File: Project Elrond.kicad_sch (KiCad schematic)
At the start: 23 parts, among them U1 OPA827, U2 OPA827, U3 OPA827

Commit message: Remove OS-specific file paths from kicad_sch
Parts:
- U1, U2, U3: Spice_Lib_File spice\OPA827.LIB -> OPA827.LIB
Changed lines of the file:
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@@
       (effects (font (size 1.27 1.27)) hide)
     )
-    (property "Spice_Lib_File" "spice\\OPA827.LIB" (id 7) (at 76.2 98.425 0)
+    (property "Spice_Lib_File" "OPA827.LIB" (id 7) (at 76.2 98.425 0)
       (effects (font (size 1.27 1.27)) hide)
     )
@@
       (effects (font (size 1.27 1.27)) hide)
     )
-    (property "Spice_Lib_File" "spice\\OPA827.LIB" (id 7) (at 160.02 100.965 0)
+    (property "Spice_Lib_File" "OPA827.LIB" (id 7) (at 160.02 100.965 0)
       (effects (font (size 1.27 1.27)) hide)
     )
@@
       (effects (font (size 1.27 1.27)) hide)
     )
-    (property "Spice_Lib_File" "spice\\OPA827.LIB" (id 7) (at 243.84 103.505 0)
+    (property "Spice_Lib_File" "OPA827.LIB" (id 7) (at 243.84 103.505 0)
       (effects (font (size 1.27 1.27)) hide)
     )

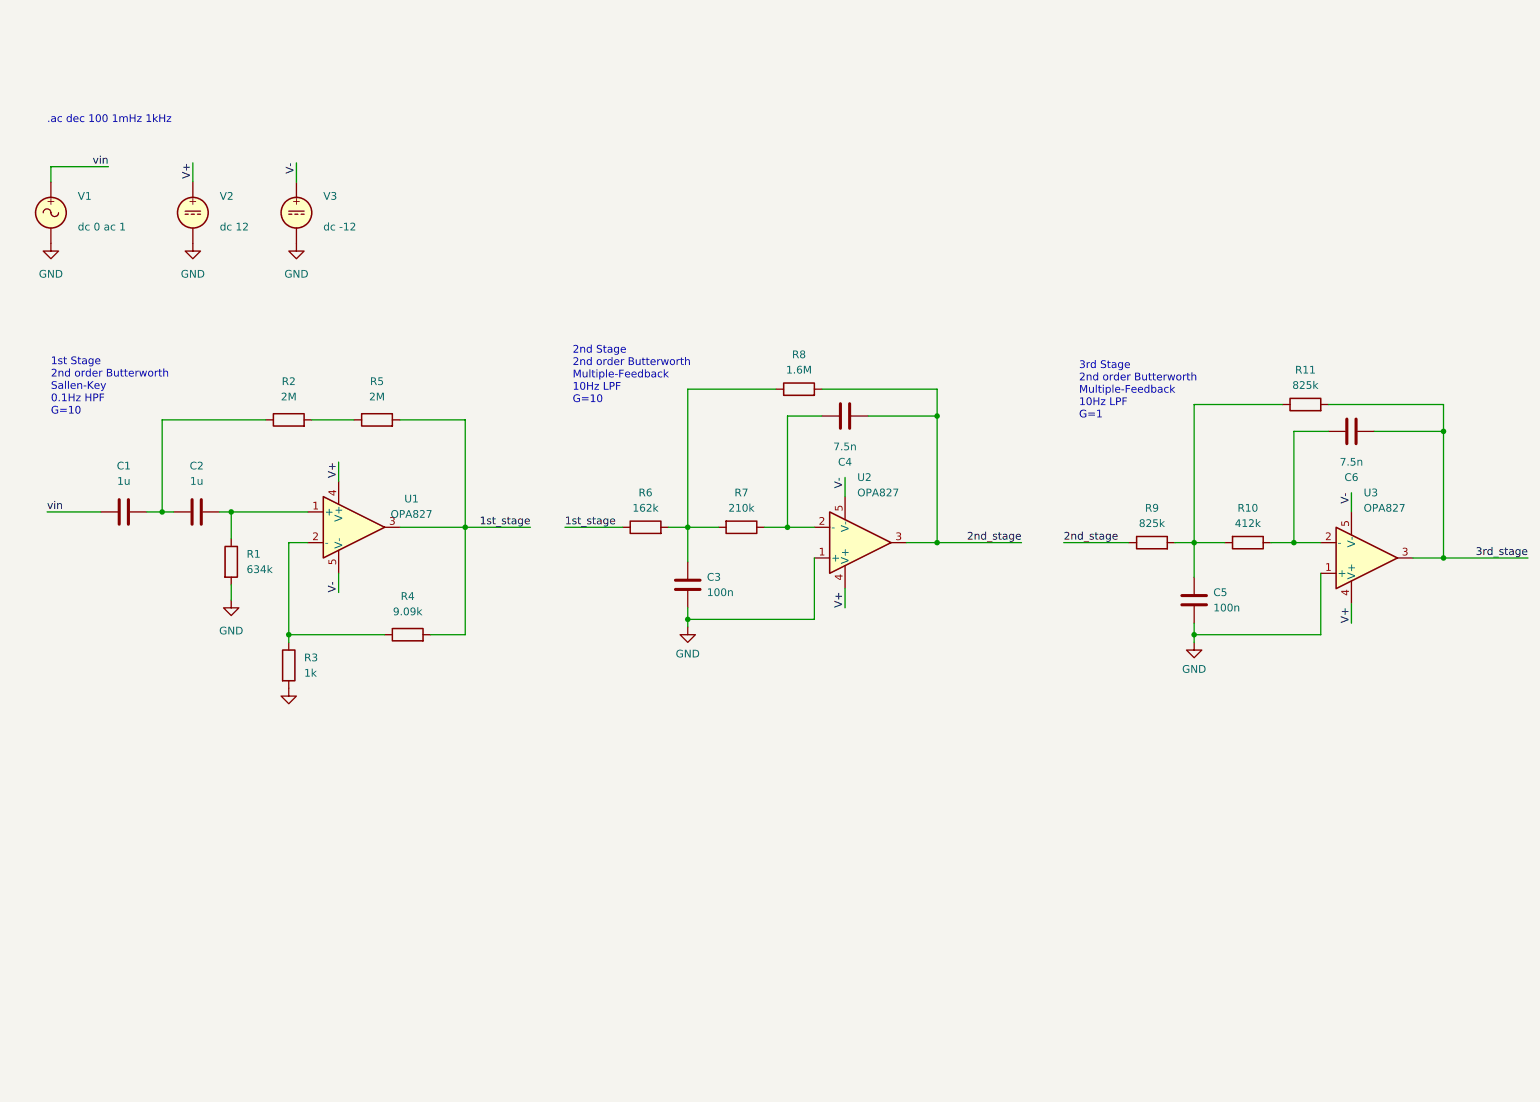
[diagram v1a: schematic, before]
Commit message: Use UA741 instead of the pricier OPA amplifier
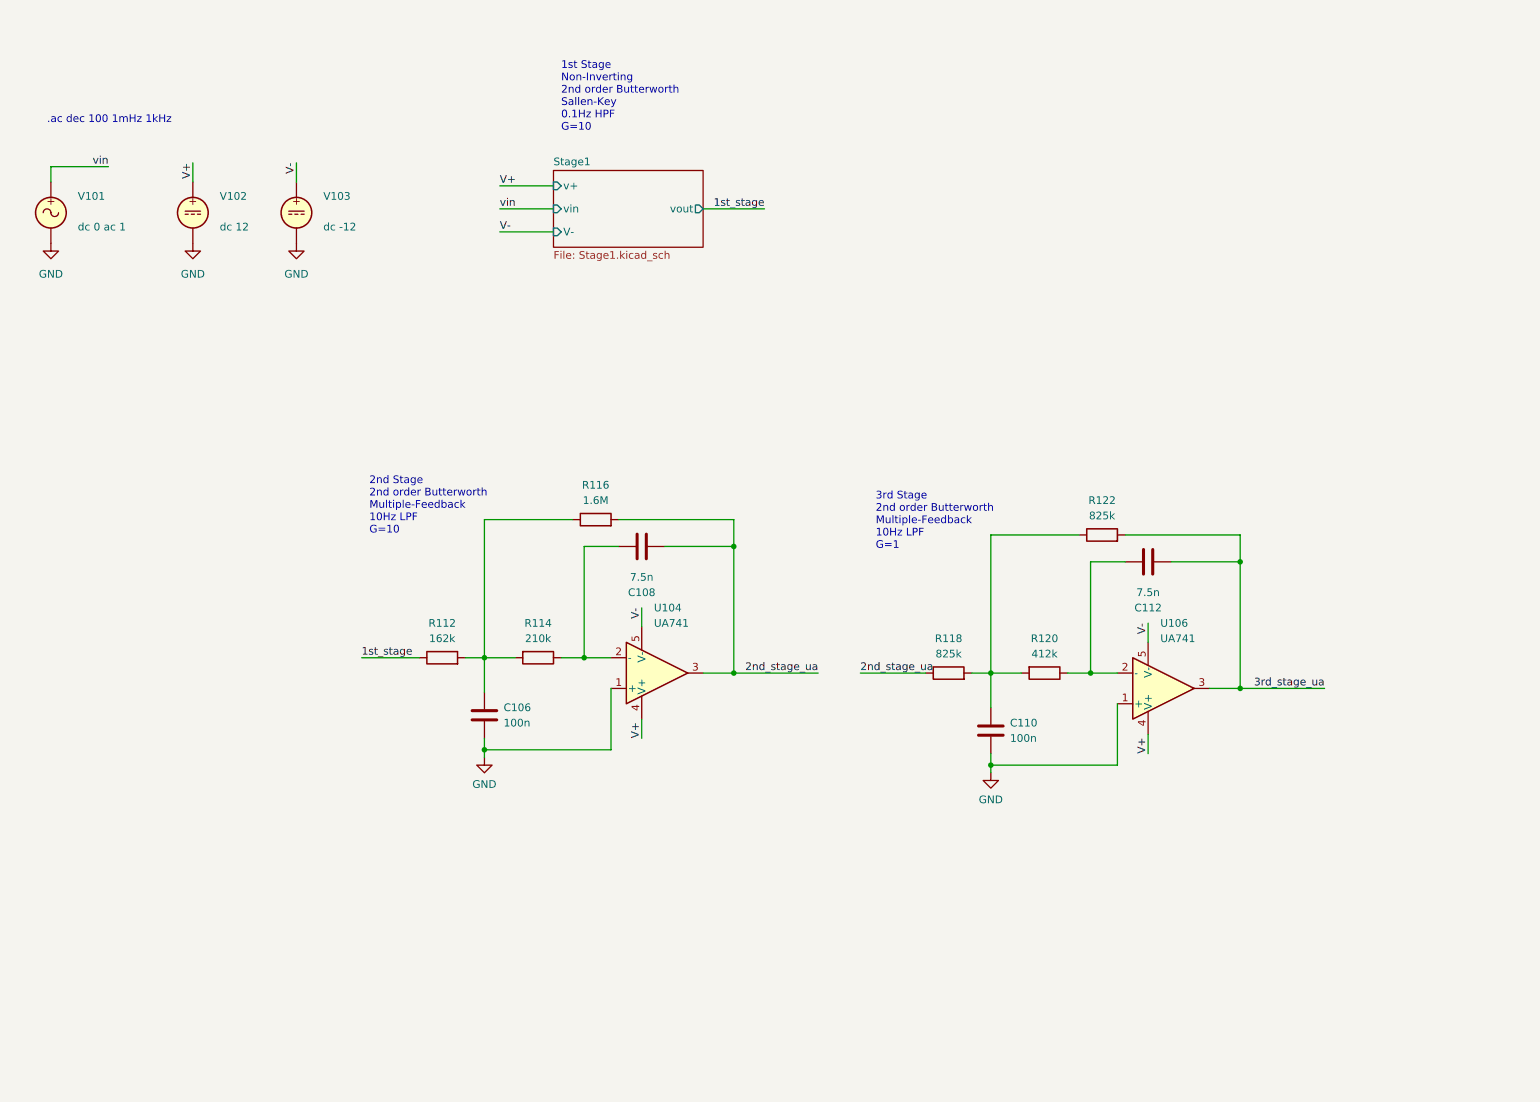
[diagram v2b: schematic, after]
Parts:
- removed C1, C2: 1u, symbol Device:C
- removed C3, C5: 100n, symbol Device:C
- removed C4, C6: 7.5n, symbol Device:C
- removed R1: 634k, symbol Device:R
- removed R10: 412k, symbol Device:R
- removed R11, R9: 825k, symbol Device:R
- removed R2, R5: 2M, symbol Device:R
- removed R3: 1k, symbol Device:R
- removed R4: 9.09k, symbol Device:R
- removed R6: 162k, symbol Device:R
- removed R7: 210k, symbol Device:R
- removed R8: 1.6M, symbol Device:R
- removed U1, U2, U3: OPA827, symbol Simulation_SPICE:OPAMP
- added C106, C110: 100n, symbol Device:C
- added C108, C112: 7.5n, symbol Device:C
- added R112: 162k, symbol Device:R
- added R114: 210k, symbol Device:R
- added R116: 1.6M, symbol Device:R
- added R118, R122: 825k, symbol Device:R
- added R120: 412k, symbol Device:R
- added U104, U106: UA741, symbol Simulation_SPICE:OPAMP
- renumbered V1 to V101, V2 to V102, V3 to V103
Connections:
- net 1st_stage: now also R112.1
- net GND: now also C106.2, C110.2, U104.1 (+), U106.1 (+)
- net V+: now also U104.4 (V+), U106.4 (V+)
- net V-: now also U104.5 (V-), U106.5 (V-)
- new net: C110.1, R118.2, R120.2, R122.1
- new net: C112.1, R120.1, U106.2 (-)
- new net: C108.1, R114.1, U104.2 (-)
- new net: C106.1, R112.2, R114.2, R116.1
- new net 2nd_stage_ua: C108.2, R116.2, R118.1, U104.3
- new net 3rd_stage_ua: C112.2, R122.2, U106.3
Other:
- added sheet Stage1 (Stage1.kicad_sch)
- note added: "1st Stage Non-Inverting 2nd order Butterworth Sallen-Key 0.1Hz HPF G=10"
- note removed: "1st Stage 2nd order Butterworth Sallen-Key 0.1Hz HPF G=10"

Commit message: Present an initial structure for multiple simulation support
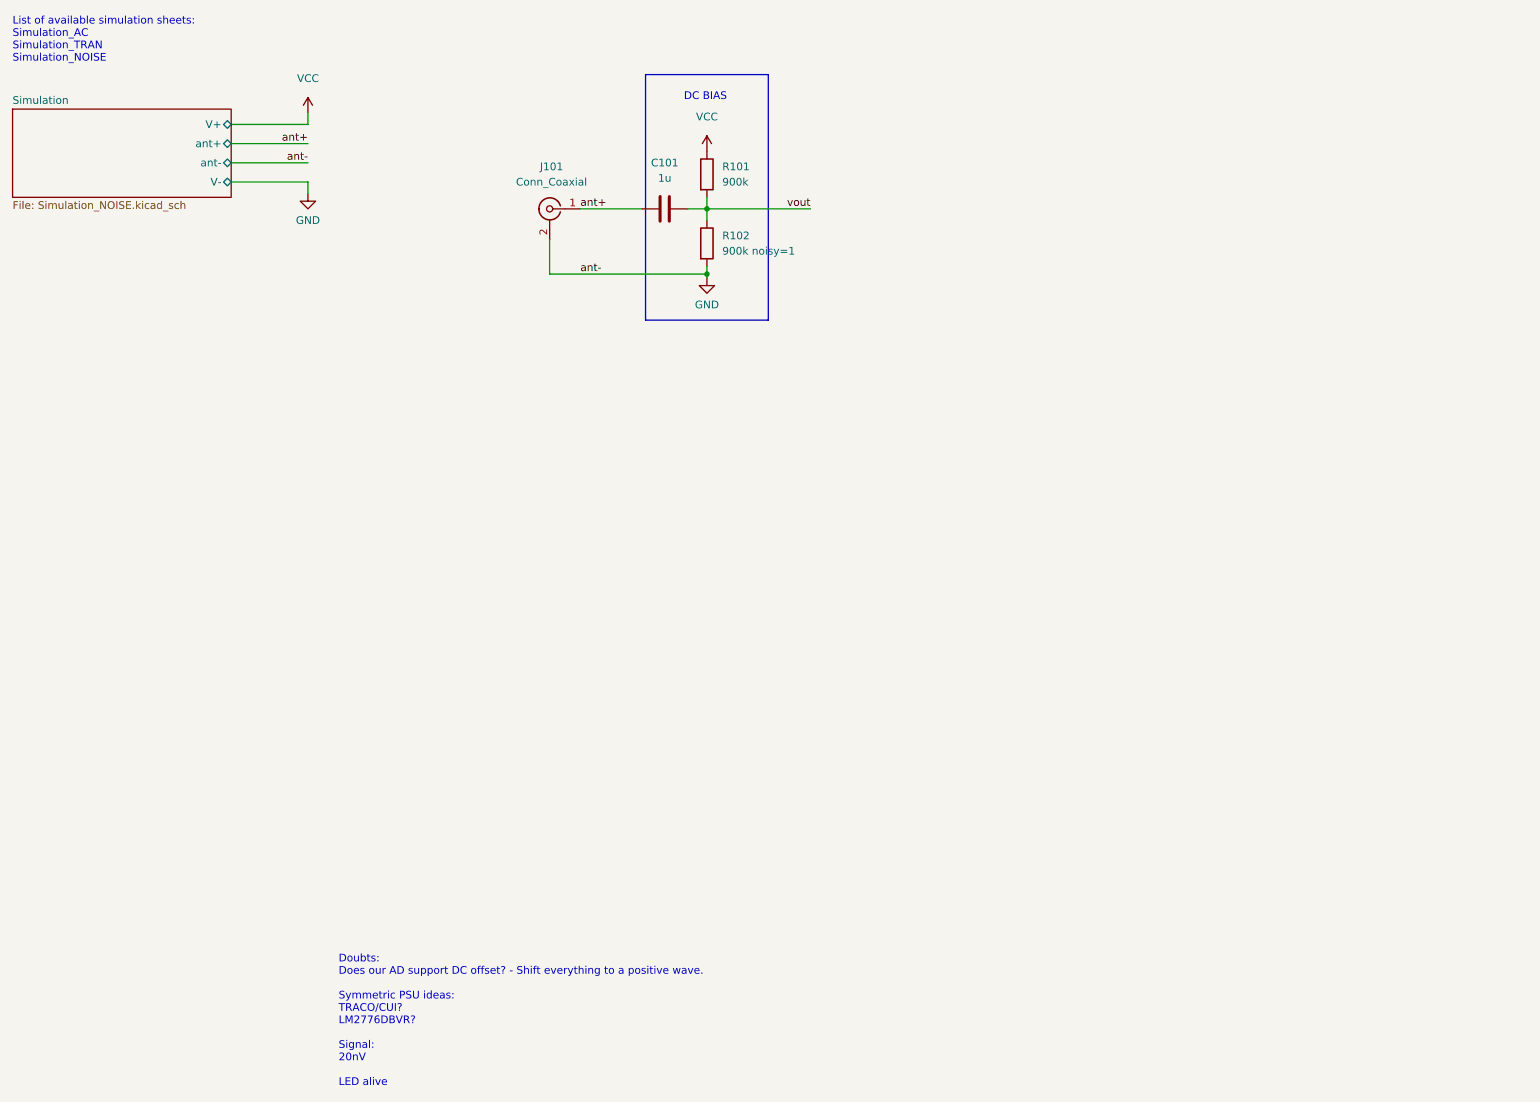
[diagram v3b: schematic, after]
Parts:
- removed C106, C110: 100n, symbol Device:C
- removed C108, C112: 7.5n, symbol Device:C
- removed R112: 162k, symbol Device:R
- removed R114: 210k, symbol Device:R
- removed R116: 1.6M, symbol Device:R
- removed R118, R122: 825k, symbol Device:R
- removed R120: 412k, symbol Device:R
- removed U104, U106: UA741, symbol Simulation_SPICE:OPAMP
- removed V101: ~, symbol Simulation_SPICE:VSIN
- removed V102, V103: ~, symbol Simulation_SPICE:VDC
- added C101: 1u, symbol Device:C
- added J101: Conn_Coaxial, symbol Connector:Conn_Coaxial
- added R101: 900k, symbol Device:R
- added R102: 900k noisy=1, symbol Device:R
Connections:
- net GND: now also J101.2 (Ext), R102.2
- new net VCC: R101.1
- new net ant+: C101.1, J101.1 (In)
- new net vout: C101.2, R101.2, R102.1
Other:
- removed sheet Stage1
- added sheet Simulation (Simulation_NOISE.kicad_sch)
- note added: "DC BIAS"
- note added: "Doubts: Does our AD support DC offset? - Shift everything to a positive wave. Symmetric PSU ideas: TRACO/CUI? LM2776DBVR? Signal: 20nV LED alive"
- note added: "List of available simulation sheets: Simulation_AC Simulation_TRAN Simulation_NOISE"
- note removed: ".ac dec 100 1mHz 1kHz"
- note removed: "1st Stage Non-Inverting 2nd order Butterworth Sallen-Key 0.1Hz HPF G=10"
- note removed: "2nd Stage 2nd order Butterworth Multiple-Feedback 10Hz LPF G=10"
- note removed: "3rd Stage 2nd order Butterworth Multiple-Feedback 10Hz LPF G=1"

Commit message: Sim tests
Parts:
- R101: Spice_Model 900k noisy=1 -> 900k
- R102: value 900k noisy=1 -> 900k; Spice_Model (none) -> 900k; Spice_Netlist_Enabled (none) -> Y; Spice_Primitive (none) -> R
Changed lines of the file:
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@@
       (effects (font (size 1.27 1.27)) hide)
     )
-    (property "Spice_Model" "900k noisy=1" (id 5) (at 134.62 40.005 0)
+    (property "Spice_Model" "900k" (id 5) (at 134.62 40.005 0)
       (effects (font (size 1.27 1.27)) hide)
     )
@@
       (effects (font (size 1.27 1.27)) (justify left))
     )
-    (property "Value" "900k noisy=1" (id 1) (at 137.16 52.7049 0)
+    (property "Value" "900k" (id 1) (at 137.16 52.7049 0)
       (effects (font (size 1.27 1.27)) (justify left))
     )
@@
     )
     (property "Datasheet" "~" (id 3) (at 134.62 51.435 0)
+      (effects (font (size 1.27 1.27)) hide)
+    )
+    (property "Spice_Primitive" "R" (id 4) (at 134.62 51.435 0)
+      (effects (font (size 1.27 1.27)) hide)
+    )
+    (property "Spice_Model" "900k" (id 5) (at 134.62 51.435 0)
+      (effects (font (size 1.27 1.27)) hide)
+    )
+    (property "Spice_Netlist_Enabled" "Y" (id 6) (at 134.62 51.435 0)
       (effects (font (size 1.27 1.27)) hide)
     )
@@
   (symbol (lib_id "power:VCC") (at 134.62 36.195 0) (unit 1)
     (in_bom yes) (on_board yes) (fields_autoplaced)
-    (property "Reference" "#PWR?" (id 0) (at 134.62 40.005 0)
+    (property "Reference" "#PWR0102" (id 0) (at 134.62 40.005 0)
       (effects (font (size 1.27 1.27)) hide)
     )
@@
   (symbol (lib_id "power:VCC") (at 68.58 29.845 0) (unit 1)
     (in_bom yes) (on_board yes) (fields_autoplaced)
-    (property "Reference" "#PWR?" (id 0) (at 68.58 33.655 0)
+    (property "Reference" "#PWR0103" (id 0) (at 68.58 33.655 0)
       (effects (font (size 1.27 1.27)) hide)
     )
@@
       (reference "#PWR0101") (unit 1) (value "GND") (footprint "")
     )
+    (path "/9e337745-cf3c-41b0-be5d-67b174a331ba"
+      (reference "#PWR0102") (unit 1) (value "VCC") (footprint "")
+    )
+    (path "/ac2f183e-e175-433b-a27f-fbe8b7213ded"
+      (reference "#PWR0103") (unit 1) (value "VCC") (footprint "")
+    )
     (path "/29f1f2e7-d9e3-4560-897e-031fd32d3741"
       (reference "#PWR0104") (unit 1) (value "GND") (footprint "")
-    )
-    (path "/9e337745-cf3c-41b0-be5d-67b174a331ba"
-      (reference "#PWR?") (unit 1) (value "VCC") (footprint "")
-    )
-    (path "/ac2f183e-e175-433b-a27f-fbe8b7213ded"
-      (reference "#PWR?") (unit 1) (value "VCC") (footprint "")
     )
     (path "/7b213714-75b5-4851-8985-ad7a896a2dc6"
@@
     )
     (path "/5400862a-a64b-46af-8ca7-fe3a71ab0d64"
-      (reference "R102") (unit 1) (value "900k noisy=1") (footprint "")
+      (reference "R102") (unit 1) (value "900k") (footprint "")
     )
     (path "/ec123445-d50c-4491-b8c0-17b89386fa17/0d3bb0af-d1a1-4aa4-afd2-b296070073ac"

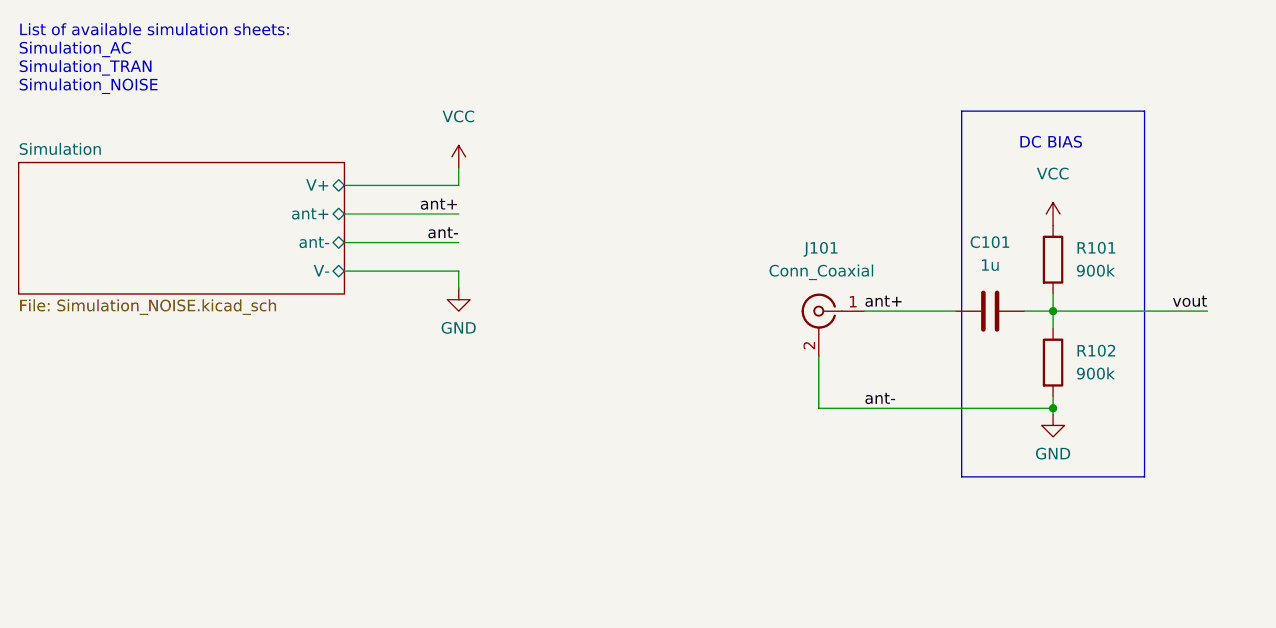
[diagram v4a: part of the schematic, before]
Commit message: Fix simulation primitives and document simulation types
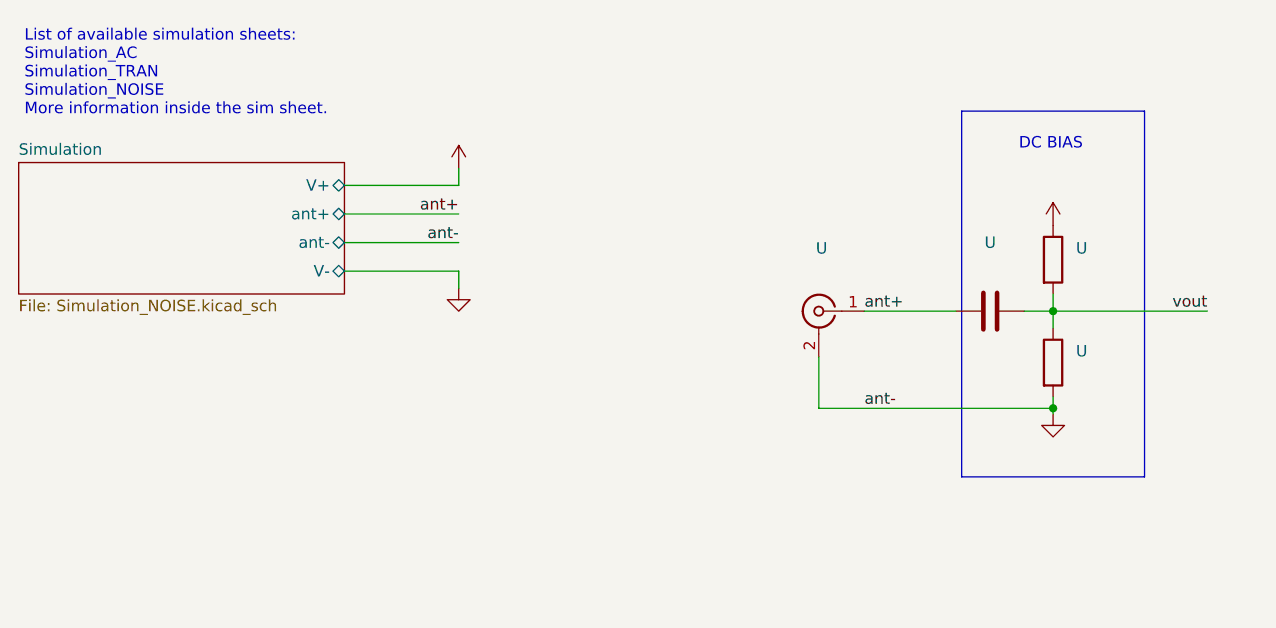
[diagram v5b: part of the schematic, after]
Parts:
- U: renamed from R101; value 900k -> (none)
- U: renamed from R102; value 900k -> (none)
- U: renamed from C101; value 1u -> (none)
- U: renamed from J101; value Conn_Coaxial -> (none)
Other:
- note added: "List of available simulation sheets: Simulation_AC Simulation_TRAN Simulation_NOISE More information inside the sim sheet."
- note removed: "List of available simulation sheets: Simulation_AC Simulation_TRAN Simulation_NOISE"
